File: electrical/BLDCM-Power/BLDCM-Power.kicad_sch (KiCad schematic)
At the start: 37 parts, among them J1 501920-3001, J2 53048-0310, J3 53261-0471, J4 53261-0471, J5 FTSH-107-01-L-DV-K, J6 12402012E212A, U1 INA239-Q1, U2 LDL212PV33R, U3 TMC6300-LA, U4 INA239-Q1, U5 TCAN1462, U6 INA239-Q1

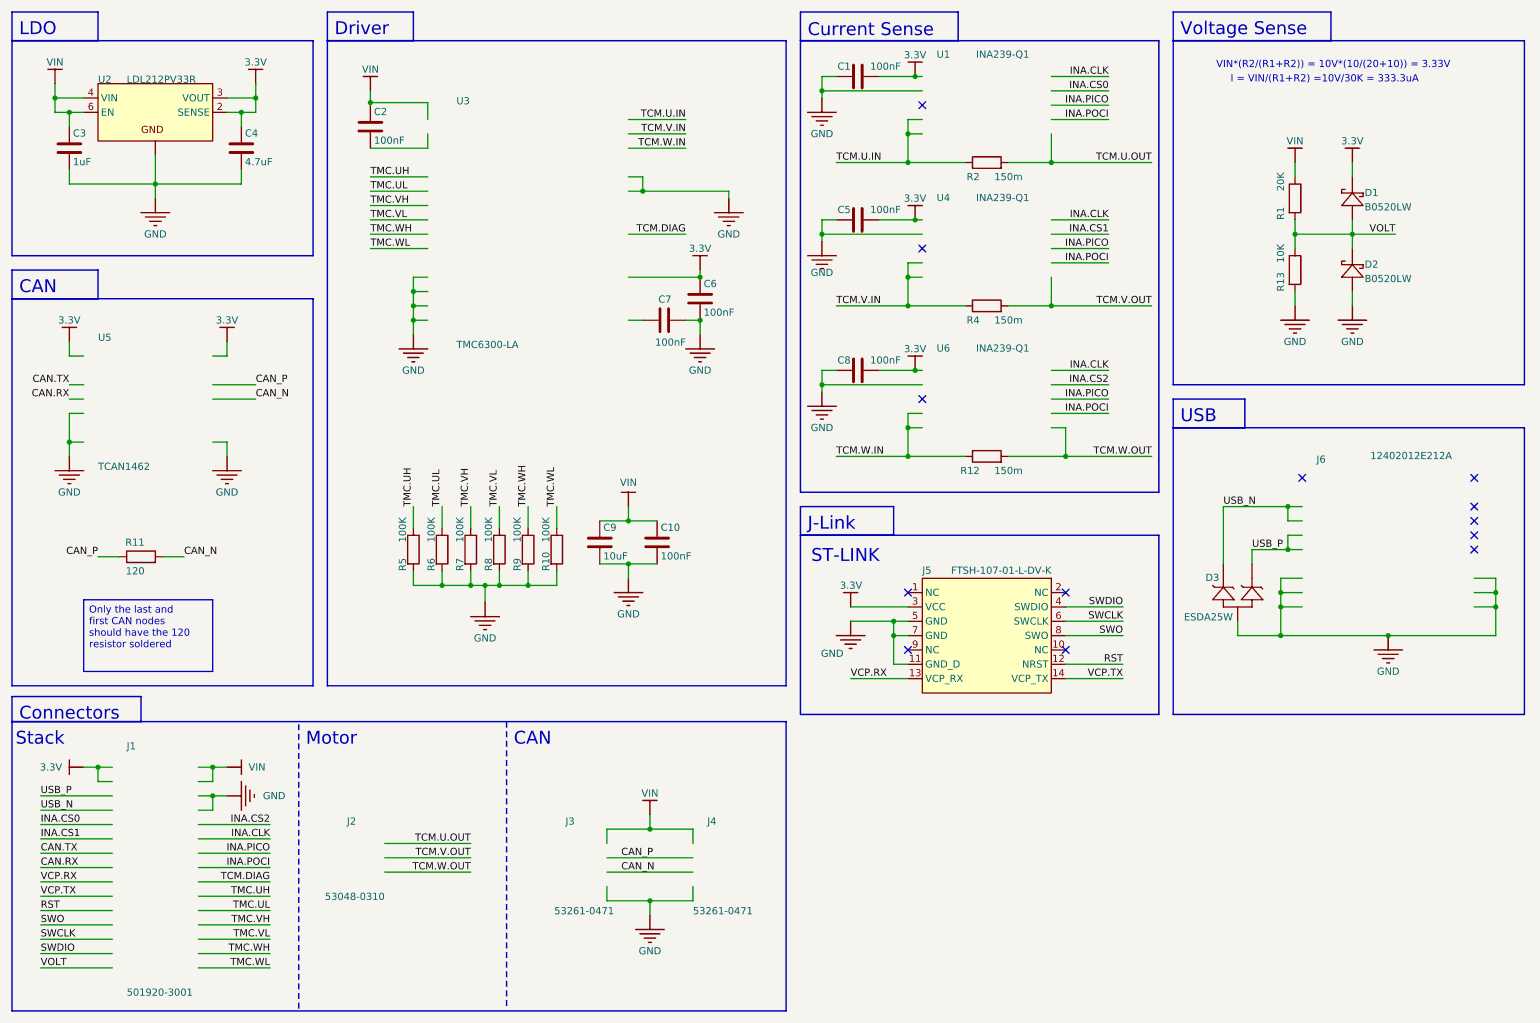
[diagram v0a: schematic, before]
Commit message: Fix: BLDCM-Power ERC errors
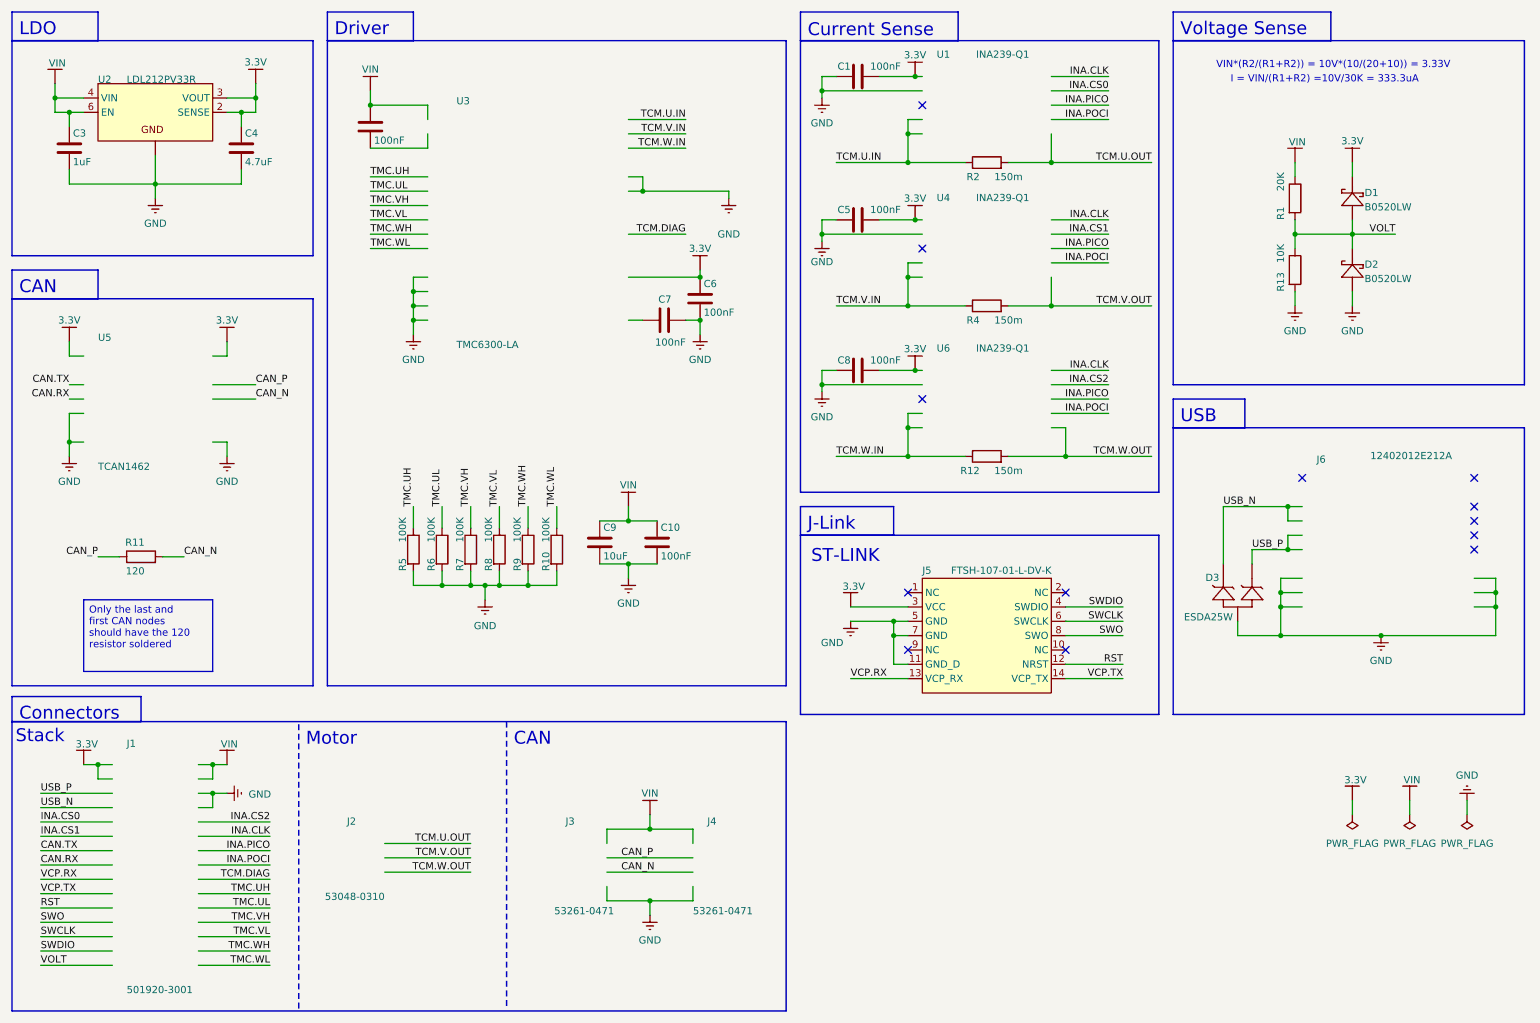
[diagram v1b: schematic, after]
